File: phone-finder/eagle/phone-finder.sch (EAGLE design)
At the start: 46 parts, among them J1 MICRO USB, J2 PHONE-JACK, K1 RELAY, Q1 12Mhz, Q2 2N2222, Q3 2N2222, T1 DTA114EET1G (2x10K), U1 AP2114H-3.3TRG1, U2 NUF2042XV6T1G, U3 LPC11U35FHI33/501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

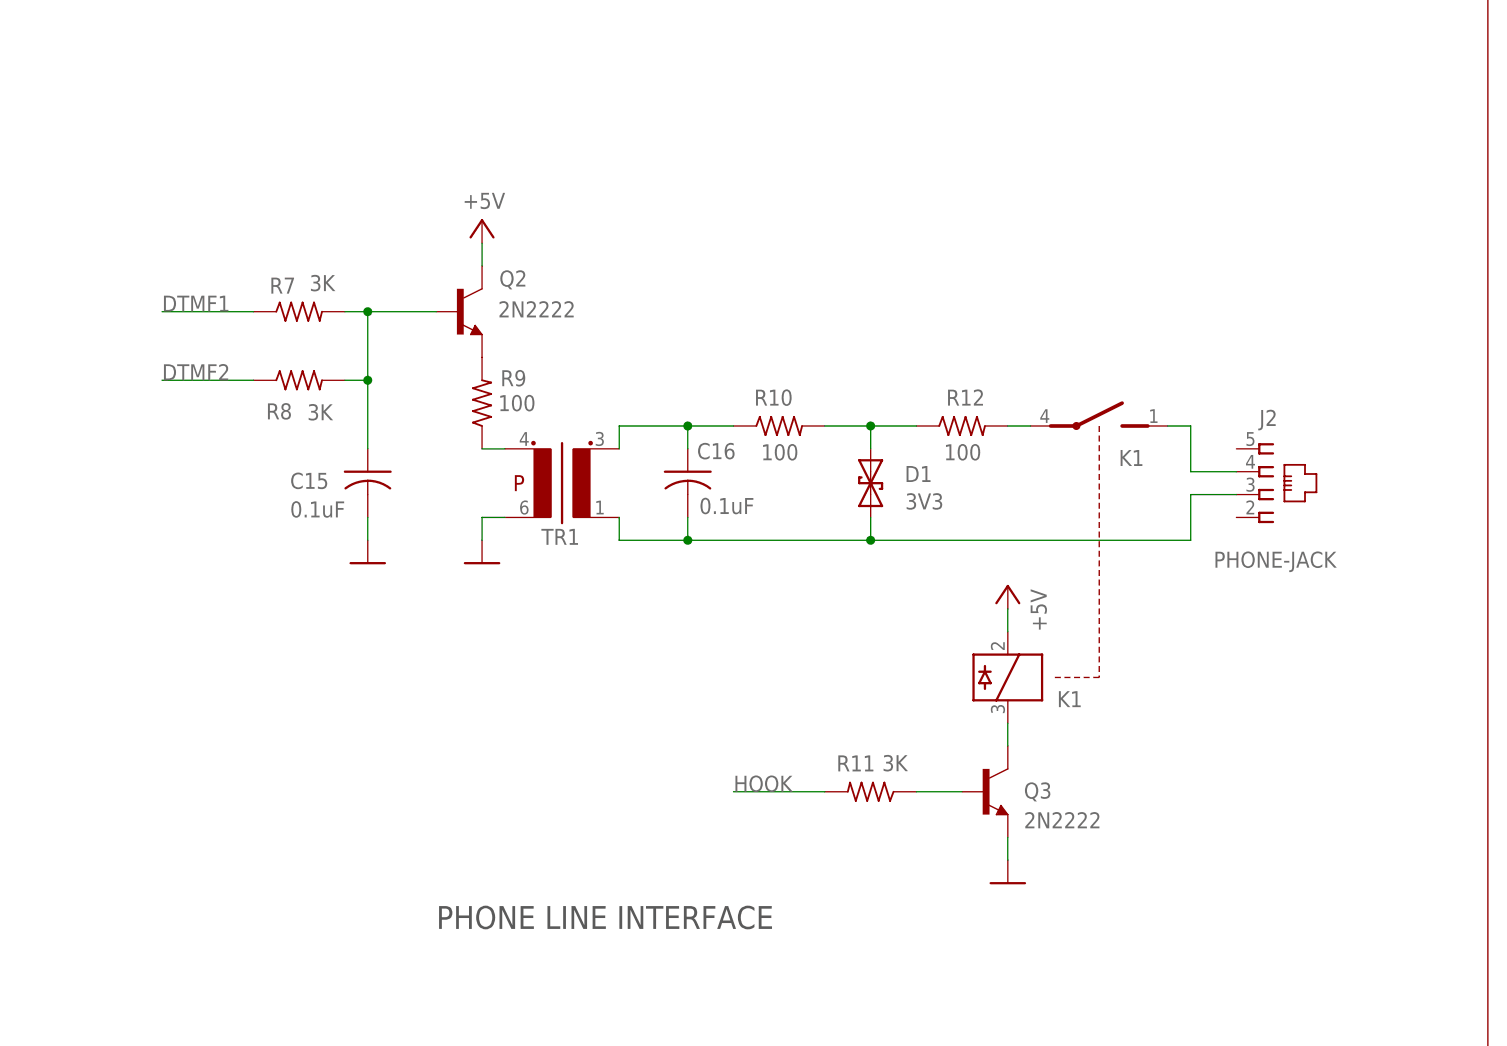
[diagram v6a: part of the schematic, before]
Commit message: Updated BOM (still needs Mouser part numbers and part references).
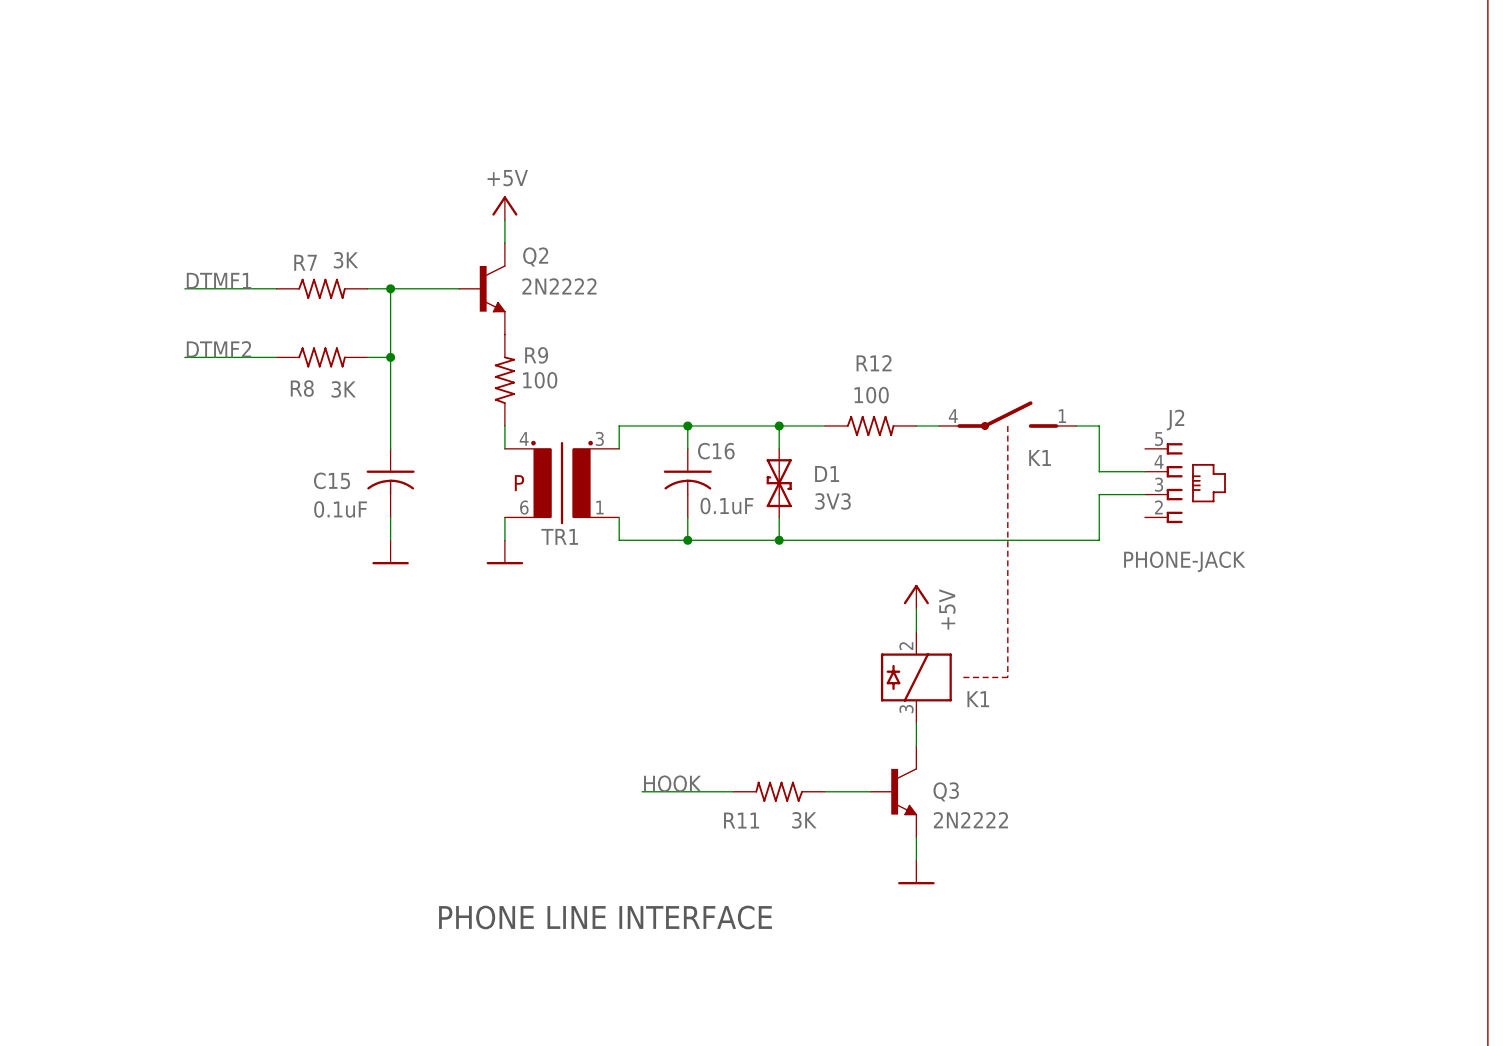
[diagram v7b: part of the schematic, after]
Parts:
- removed R10: 100, phone-finder:RR0805
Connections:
- removed net N$15: D1.2, R10.2, R12.1
- net N$9: now also D1.2, R12.1; no longer R10.1
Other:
- moved on the sheet: C15, D1, J2, K1, Q2, Q3, R11, R12, R7, R8, R9

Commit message: PCB layout in progress.
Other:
- note added: "LED"
- moved on the sheet: C15, C16, C17, C5, C6, C7, C8, D1, D2, D3, J1, J2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
